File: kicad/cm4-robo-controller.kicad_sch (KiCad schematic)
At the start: 4 parts, among them U1 ROBOCLAW-2X15A-OEM, U10 KF7620-7.62-2P

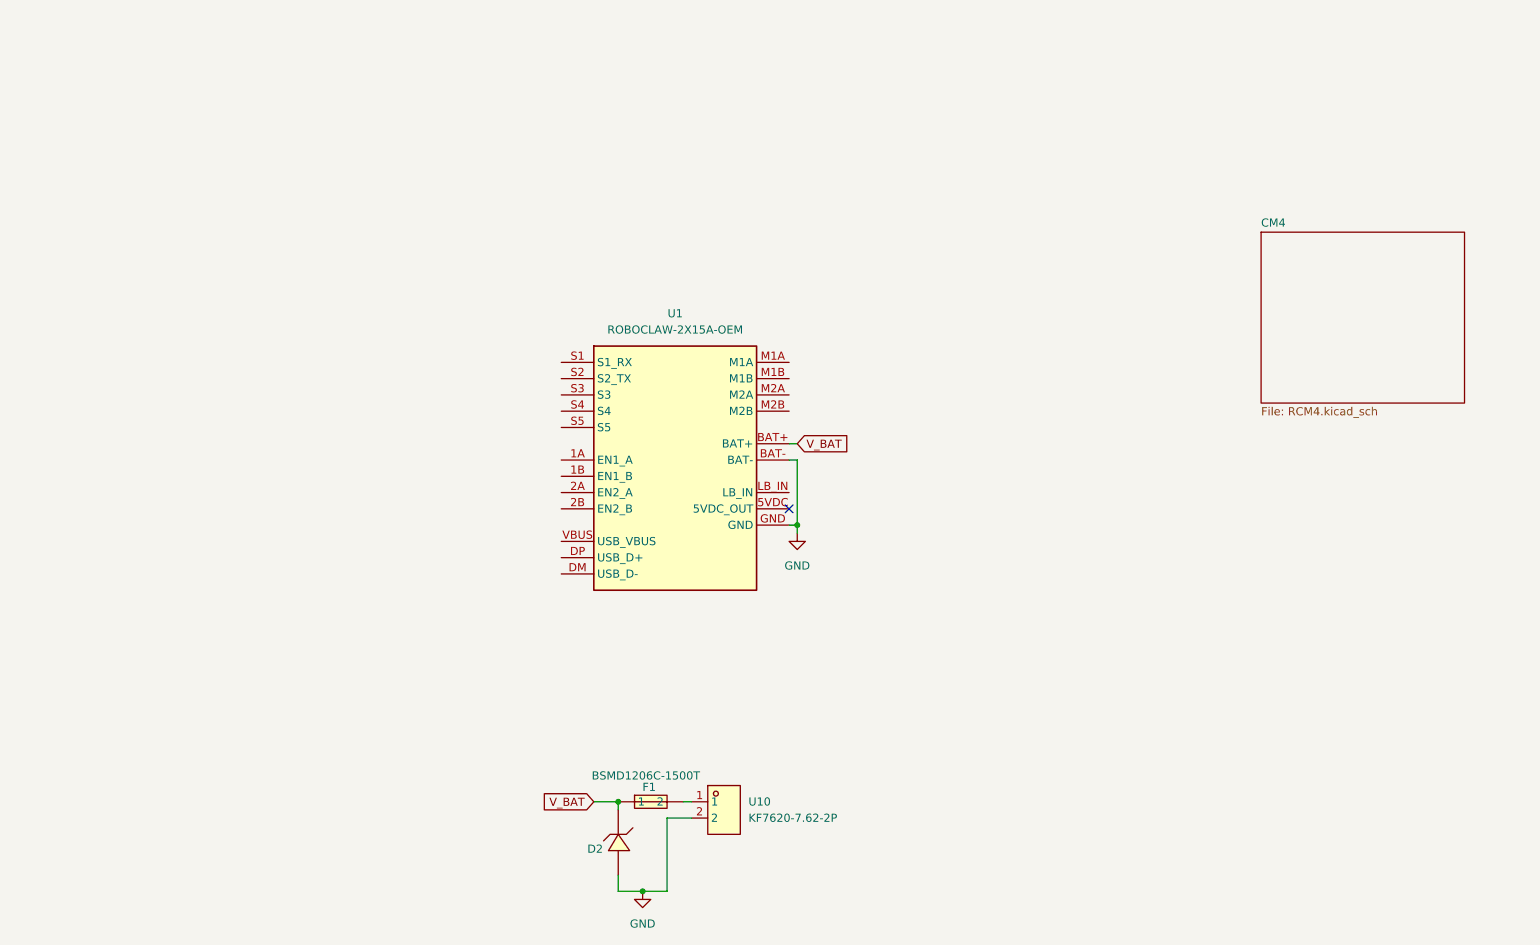
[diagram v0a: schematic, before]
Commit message: GPIO connectors defined
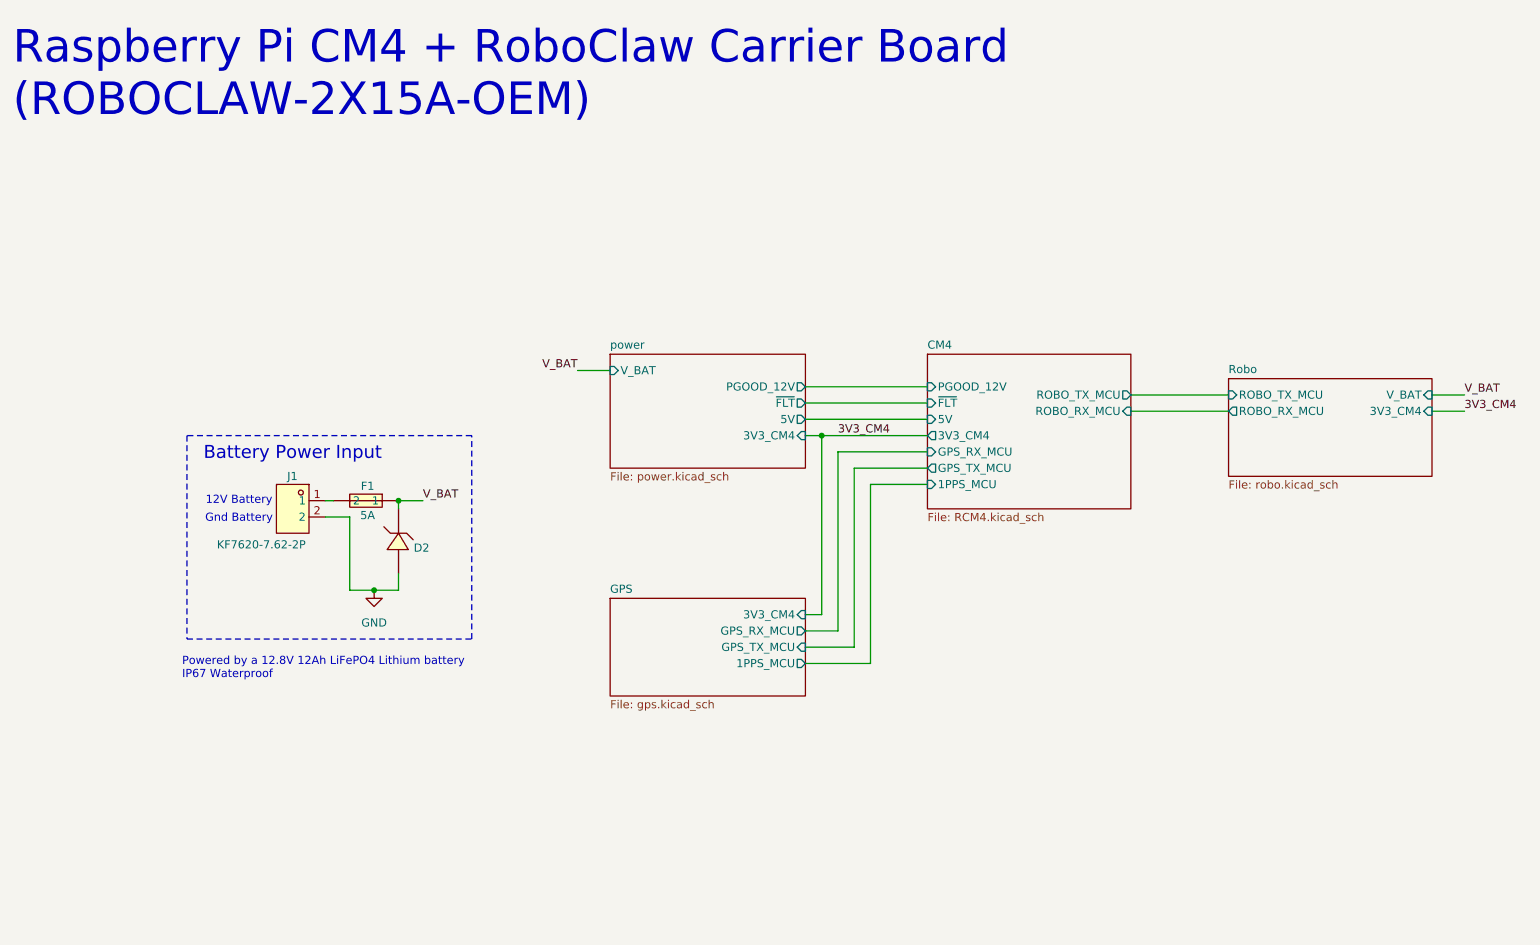
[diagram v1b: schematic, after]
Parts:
- removed U1: ROBOCLAW-2X15A-OEM, MyParts:MOD-TH_ROBOCLAW-OEM-2X15A, symbol MyParts:ROBOCLAW-2X15A-OEM
- D2: Manufacturer TECH PUBLIC(台舟) -> TECH PUBLIC
- F1: value BSMD1206C-1500T -> 5A; Manufacturer BHFUSE(佰宏) -> BHFUSE
- J1: renamed from U10; Manufacturer KEFA(科发) -> KEFA
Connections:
- no-connect marks 1 -> 0
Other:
- added sheet GPS (gps.kicad_sch)
- added sheet Robo (robo.kicad_sch)
- added sheet power (power.kicad_sch)
- sheet CM4 ports: added 1PPS_MCU, 3V3_CM4, 5V, GPS_RX_MCU, GPS_TX_MCU, PGOOD_12V, ROBO_RX_MCU, ROBO_TX_MCU, ~{FLT}; removed none
- note added: "12V Battery"
- note added: "Battery Power Input"
- note added: "Gnd Battery"
- note added: "Powered by a 12.8V 12Ah LiFePO4 Lithium battery IP67 Waterproof"
- note added: "Raspberry Pi CM4 + RoboClaw Carrier Board (ROBOCLAW-2X15A-OEM)"
- moved on the sheet: D2, F1, J1
